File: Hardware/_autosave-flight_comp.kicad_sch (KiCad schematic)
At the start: 29 parts, among them J2 ARM_SWD_TC2030, J4 USB_C_Receptacle_USB2.0_16P, U1 STM32F405RGTx, U4 W25Q32JVSS, U5 24LC64, U8 USBLC6-2SC6, Y1 8mHz, Y2 32.768 kHz

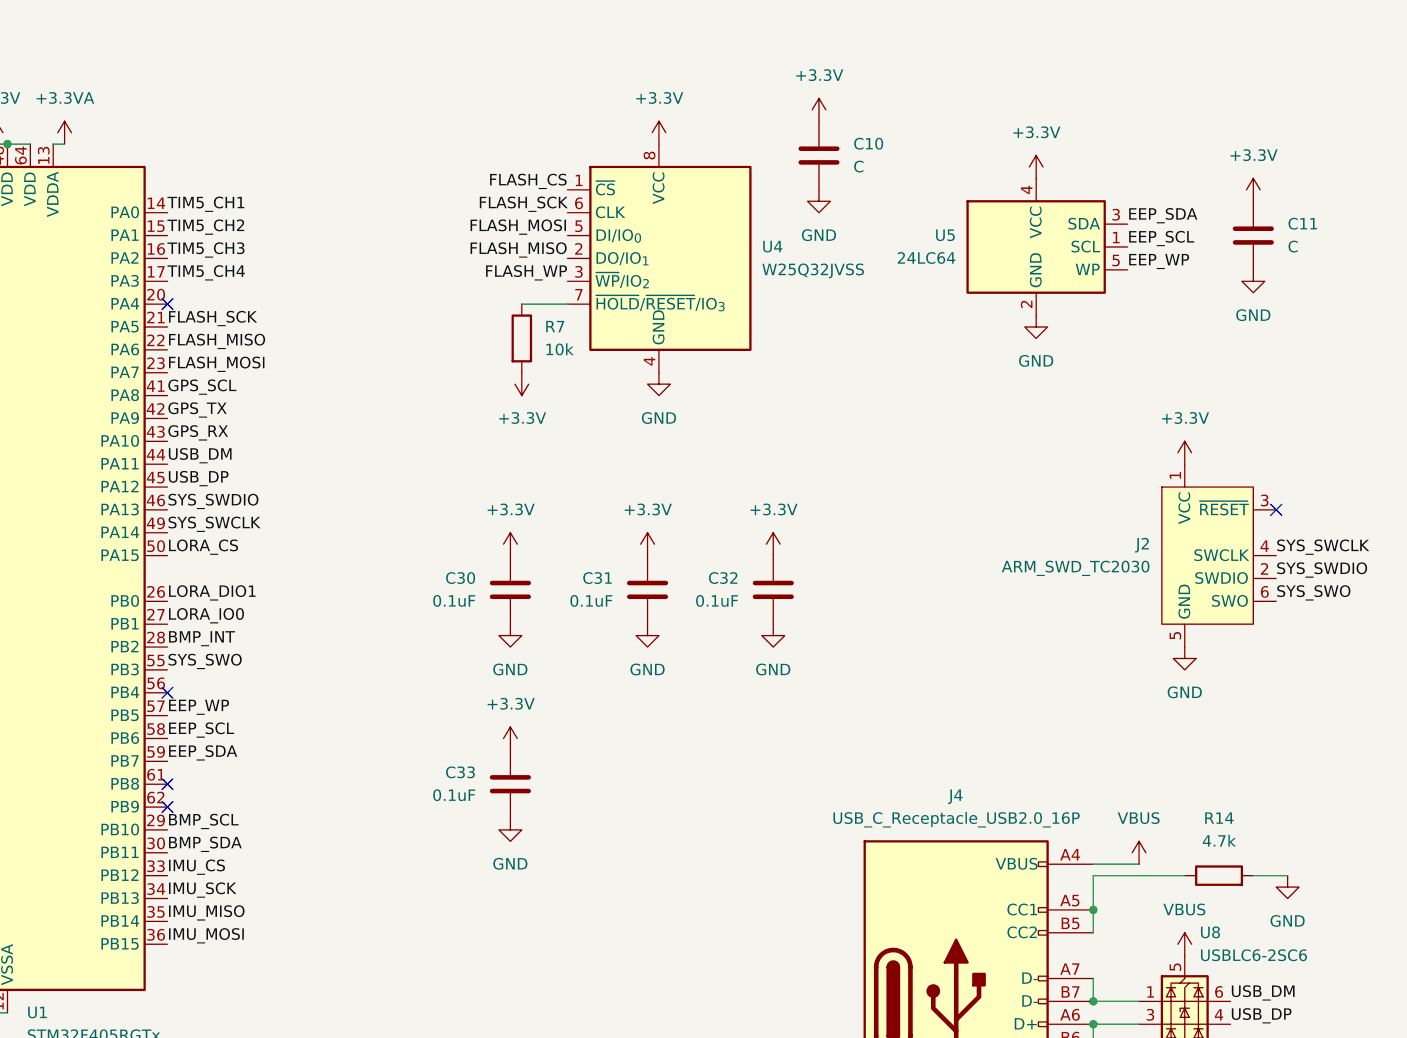
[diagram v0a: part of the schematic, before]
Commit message: pieliku IMU un vēl kaut ko
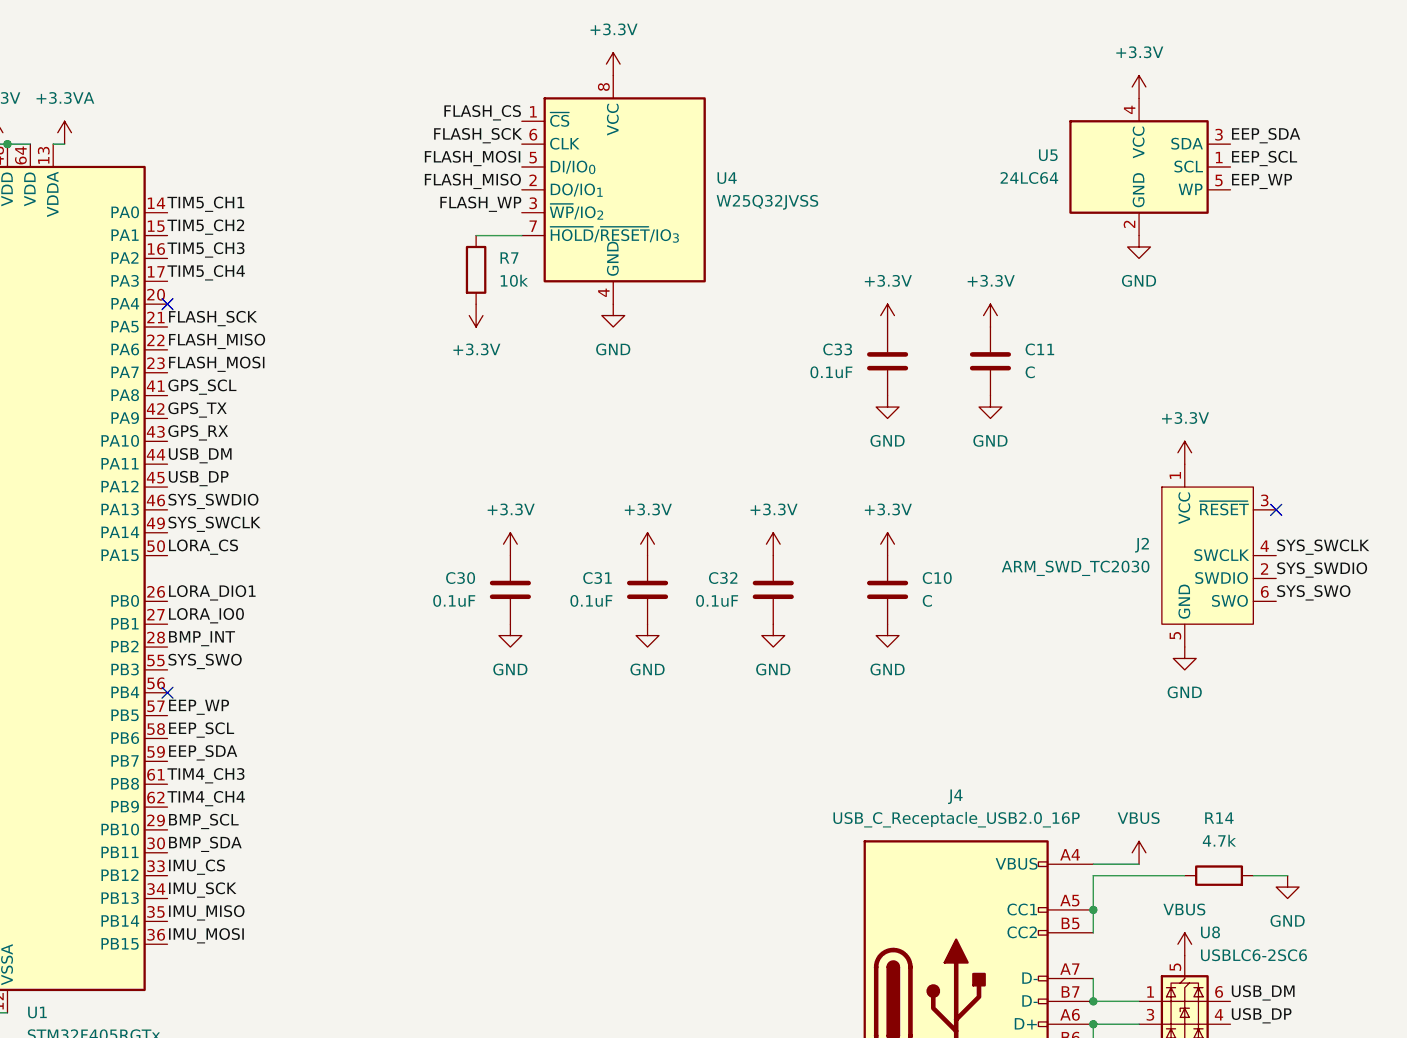
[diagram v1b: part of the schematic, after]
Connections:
- net TIM4_CH3: now reaches U1.61 (PB8)
- net TIM4_CH4: now reaches U1.62 (PB9)
- no-connect marks 11 -> 9
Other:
- moved on the sheet: C10, C11, C33, R7, U4, U5
